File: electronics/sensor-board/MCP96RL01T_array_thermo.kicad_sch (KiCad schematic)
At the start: 54 parts, among them J10 Therm_1, J11 Therm_4, J12 Therm_7, J13 Therm_2, J14 Therm_5, J15 Therm_3, J16 Therm_6, U10 MCP96RL01T, U4 MCP96RL01T, U5 MCP96RL01T, U6 MCP96RL01T, U7 MCP96RL01T, U8 MCP96RL01T, U9 MCP96RL01T

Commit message: work on sensor-board
thermocouple connector footprints made (selected connector)
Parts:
- J10, J11, J12, J13, J14, J15, J16: footprint (none) -> K_type_thermo_conn_F:K_type_thermo_conn_F
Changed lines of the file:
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@@
     (property "Reference" "J10" (id 0) (at 26.162 40.005 0))
     (property "Value" "Therm_1" (id 1) (at 27.432 48.895 0))
-    (property "Footprint" "" (id 2) (at 25.4 42.545 0)
+    (property "Footprint" "K_type_thermo_conn_F:K_type_thermo_conn_F" (id 2) (at 25.4 42.545 0)
       (effects (font (size 1.27 1.27)) hide)
     )
@@
     (property "Reference" "J11" (id 0) (at 26.162 95.885 0))
     (property "Value" "Therm_4" (id 1) (at 27.432 104.775 0))
-    (property "Footprint" "" (id 2) (at 25.4 98.425 0)
+    (property "Footprint" "K_type_thermo_conn_F:K_type_thermo_conn_F" (id 2) (at 25.4 98.425 0)
       (effects (font (size 1.27 1.27)) hide)
     )
@@
     (property "Reference" "J12" (id 0) (at 81.407 151.765 0))
     (property "Value" "Therm_7" (id 1) (at 82.677 160.655 0))
-    (property "Footprint" "" (id 2) (at 80.645 154.305 0)
+    (property "Footprint" "K_type_thermo_conn_F:K_type_thermo_conn_F" (id 2) (at 80.645 154.305 0)
       (effects (font (size 1.27 1.27)) hide)
     )
@@
     (property "Reference" "J13" (id 0) (at 108.077 40.005 0))
     (property "Value" "Therm_2" (id 1) (at 109.347 48.895 0))
-    (property "Footprint" "" (id 2) (at 107.315 42.545 0)
+    (property "Footprint" "K_type_thermo_conn_F:K_type_thermo_conn_F" (id 2) (at 107.315 42.545 0)
       (effects (font (size 1.27 1.27)) hide)
     )
@@
     (property "Reference" "J14" (id 0) (at 108.077 95.885 0))
     (property "Value" "Therm_5" (id 1) (at 109.347 104.775 0))
-    (property "Footprint" "" (id 2) (at 107.315 98.425 0)
+    (property "Footprint" "K_type_thermo_conn_F:K_type_thermo_conn_F" (id 2) (at 107.315 98.425 0)
       (effects (font (size 1.27 1.27)) hide)
     )
@@
     (property "Reference" "J15" (id 0) (at 189.992 40.005 0))
     (property "Value" "Therm_3" (id 1) (at 191.262 48.895 0))
-    (property "Footprint" "" (id 2) (at 189.23 42.545 0)
+    (property "Footprint" "K_type_thermo_conn_F:K_type_thermo_conn_F" (id 2) (at 189.23 42.545 0)
       (effects (font (size 1.27 1.27)) hide)
     )
@@
     (property "Reference" "J16" (id 0) (at 189.992 95.885 0))
     (property "Value" "Therm_6" (id 1) (at 191.262 104.775 0))
-    (property "Footprint" "" (id 2) (at 189.23 98.425 0)
+    (property "Footprint" "K_type_thermo_conn_F:K_type_thermo_conn_F" (id 2) (at 189.23 98.425 0)
       (effects (font (size 1.27 1.27)) hide)
     )

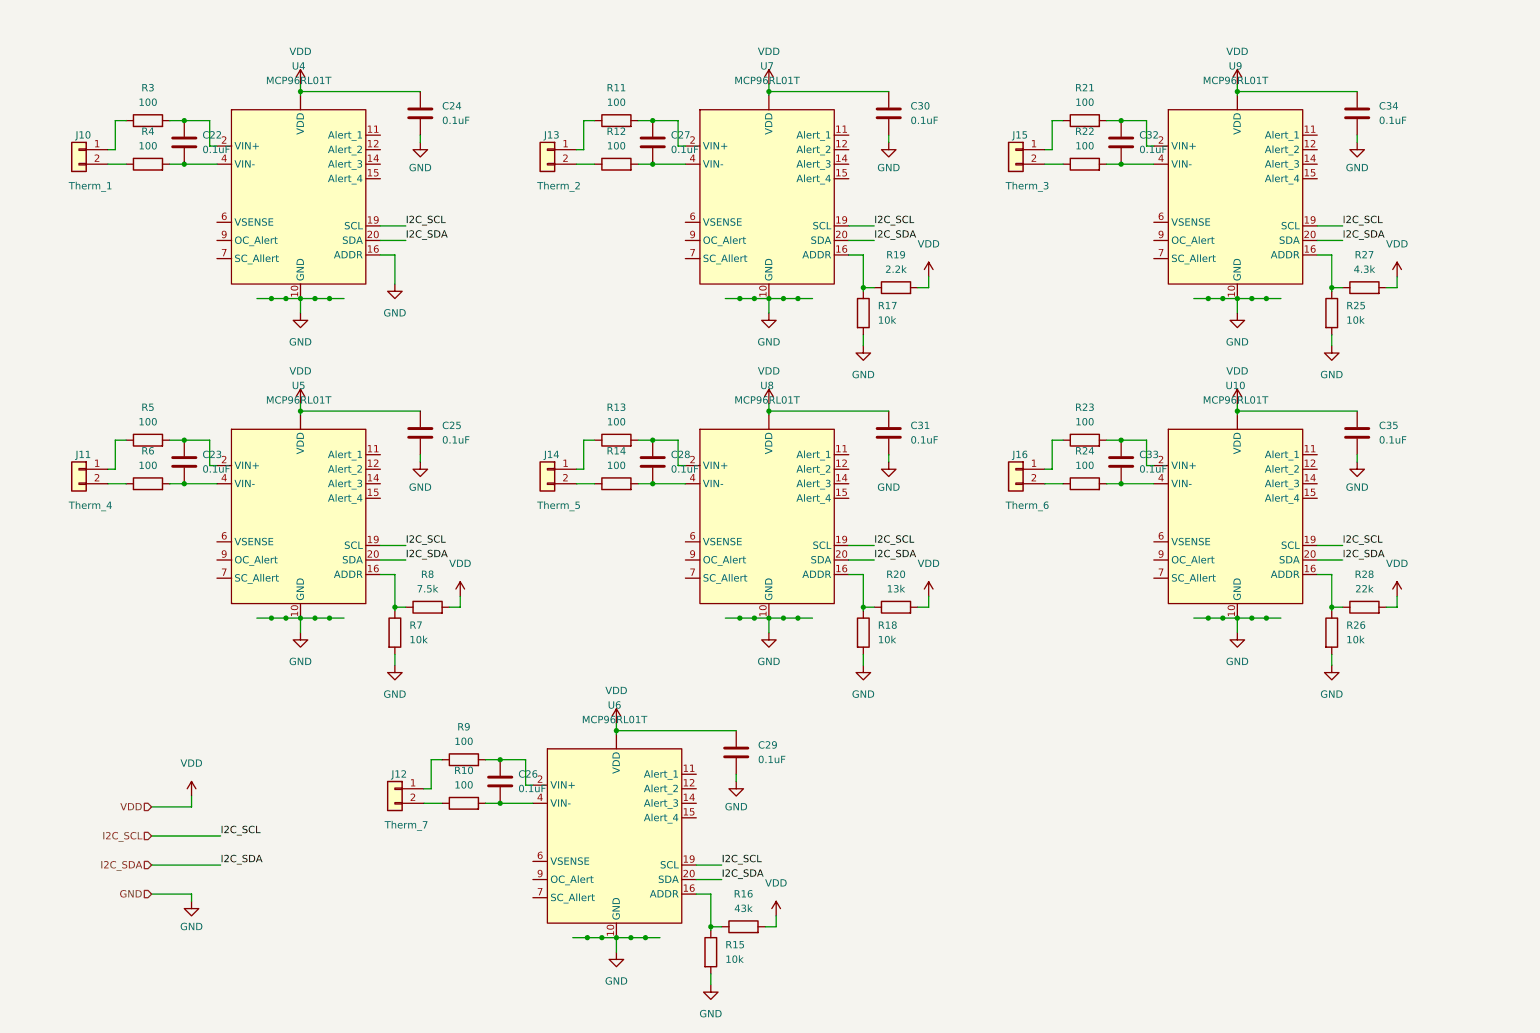
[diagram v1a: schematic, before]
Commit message: work on sensor-board
finishing sub-circuits
switching mcu to stm32f105
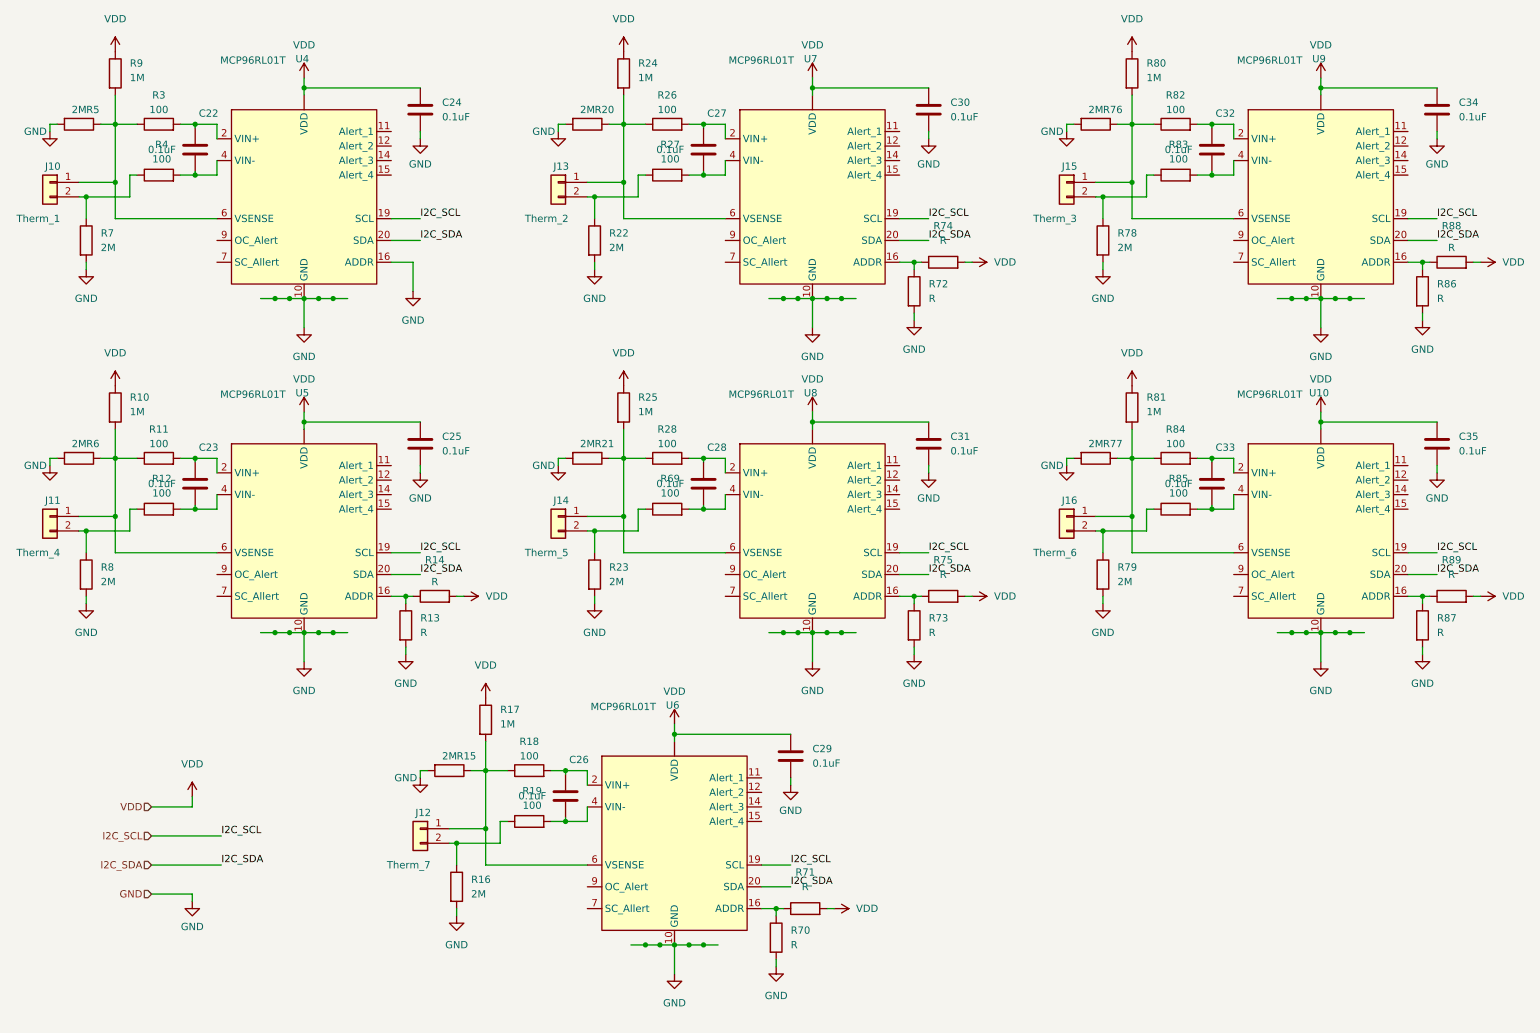
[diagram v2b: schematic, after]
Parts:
- added R69, R82, R83, R84, R85: 100, Resistor_SMD:R_0603_1608Metric, symbol Device:R
- added R70, R71, R72, R73, R74, R75, R86, R87, R88, R89: R, Resistor_SMD:R_0603_1608Metric, symbol Device:R
- added R76, R77, R78, R79: 2M, Resistor_SMD:R_0603_1608Metric, symbol Device:R
- added R80, R81: 1M, Resistor_SMD:R_0603_1608Metric, symbol Device:R
- R10, R24, R9: value 100 -> 1M
- R13, R14: value 100 -> R
- R15, R7: value 10k -> 2M
- R16: value 43k -> 2M
- R17, R25: value 10k -> 1M
- R18, R26: value 10k -> 100
- R19: value 2.2k -> 100
- R20: value 13k -> 2M
- R21, R22, R23, R5, R6: value 100 -> 2M
- R27: value 4.3k -> 100
- R28: value 22k -> 100
- R8: value 7.5k -> 2M
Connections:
- net GND: now also R13.2, R16.2, R20.2, R21.2, R22.2, R23.2, R5.2, R6.2, R8.2, R70.2, R72.2, R73.2, R76.2, R77.2, R78.2, R79.2, R86.2, R87.2; no longer R17.2, R18.2, R25.2, R26.2
- net VDD: now also R10.1, R14.2, R17.1, R24.1, R25.1, R9.1, R71.2, R74.2, R75.2, R80.1, R81.1, R88.2, R89.2; no longer R16.2, R19.2, R20.2, R27.2, R28.2, R8.2
- net at J10.2 (Pin_2), R4.1: now also R7.1
- net at R13.1: now also R14.1, U5.16 (ADDR); no longer J14.1 (Pin_1)
- net at C28.1, U8.2 (VIN+): now also R28.2; no longer R13.2
- net at C32.1, U9.2 (VIN+): now also R82.2; no longer R21.2
- net at C32.2, U9.4 (VIN-): now also R83.2; no longer R22.2
- net at R22.1: now also J13.2 (Pin_2), R27.1; no longer J15.2 (Pin_2)
- net at C33.1, U10.2 (VIN+): now also R84.2; no longer R23.2
- net at C33.2, U10.4 (VIN-): now also R85.2; no longer R24.2
- net at J16.1 (Pin_1): now also U10.6 (VSENSE), R77.1, R81.2, R84.1; no longer R23.1
- net at J14.2 (Pin_2): now also R23.1, R69.1; no longer R14.1
- net at C28.2, U8.4 (VIN-): now also R69.2; no longer R14.2
- net at U8.6 (VSENSE): now also J14.1 (Pin_1), R21.1, R25.2, R28.1
- net at C23.1, U5.2 (VIN+): now also R11.2; no longer R5.2
- net at C23.2, U5.4 (VIN-): now also R12.2; no longer R6.2
- net at U5.6 (VSENSE): now also J11.1 (Pin_1), R10.2, R11.1, R6.1
- net at J12.1 (Pin_1): now also R15.1, R17.2, R18.1, U6.6 (VSENSE); no longer R9.1
- net at J12.2 (Pin_2): now also R16.1, R19.1; no longer R10.1
- net at C27.1, U7.2 (VIN+): now also R26.2; no longer R11.2
- net at C27.2, U7.4 (VIN-): now also R27.2; no longer R12.2
- net at J11.2 (Pin_2): now also R12.1, R8.1; no longer R6.1
- net at J13.1 (Pin_1): now also R20.1, R24.2, R26.1, U7.6 (VSENSE); no longer R11.1
- net at J10.1 (Pin_1), R3.1: now also R5.1, R9.2, U4.6 (VSENSE)
- net at U9.6 (VSENSE): now also J15.1 (Pin_1), R76.1, R80.2, R82.1
- net at J16.2 (Pin_2): now also R79.1, R85.1; no longer R24.1
- net at C26.1, U6.2 (VIN+): now also R18.2; no longer R9.2
- net at C26.2, U6.4 (VIN-): now also R19.2; no longer R10.2
- new net: R70.1, R71.1, U6.16 (ADDR)
- new net: R72.1, R74.1, U7.16 (ADDR)
- new net: R87.1, R89.1, U10.16 (ADDR)
- new net: R86.1, R88.1, U9.16 (ADDR)
- new net: J15.2 (Pin_2), R78.1, R83.1
- new net: R73.1, R75.1, U8.16 (ADDR)
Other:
- moved on the sheet: C22, C24, J10, R3, R4, U4

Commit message: Finalized sensor-board schematic
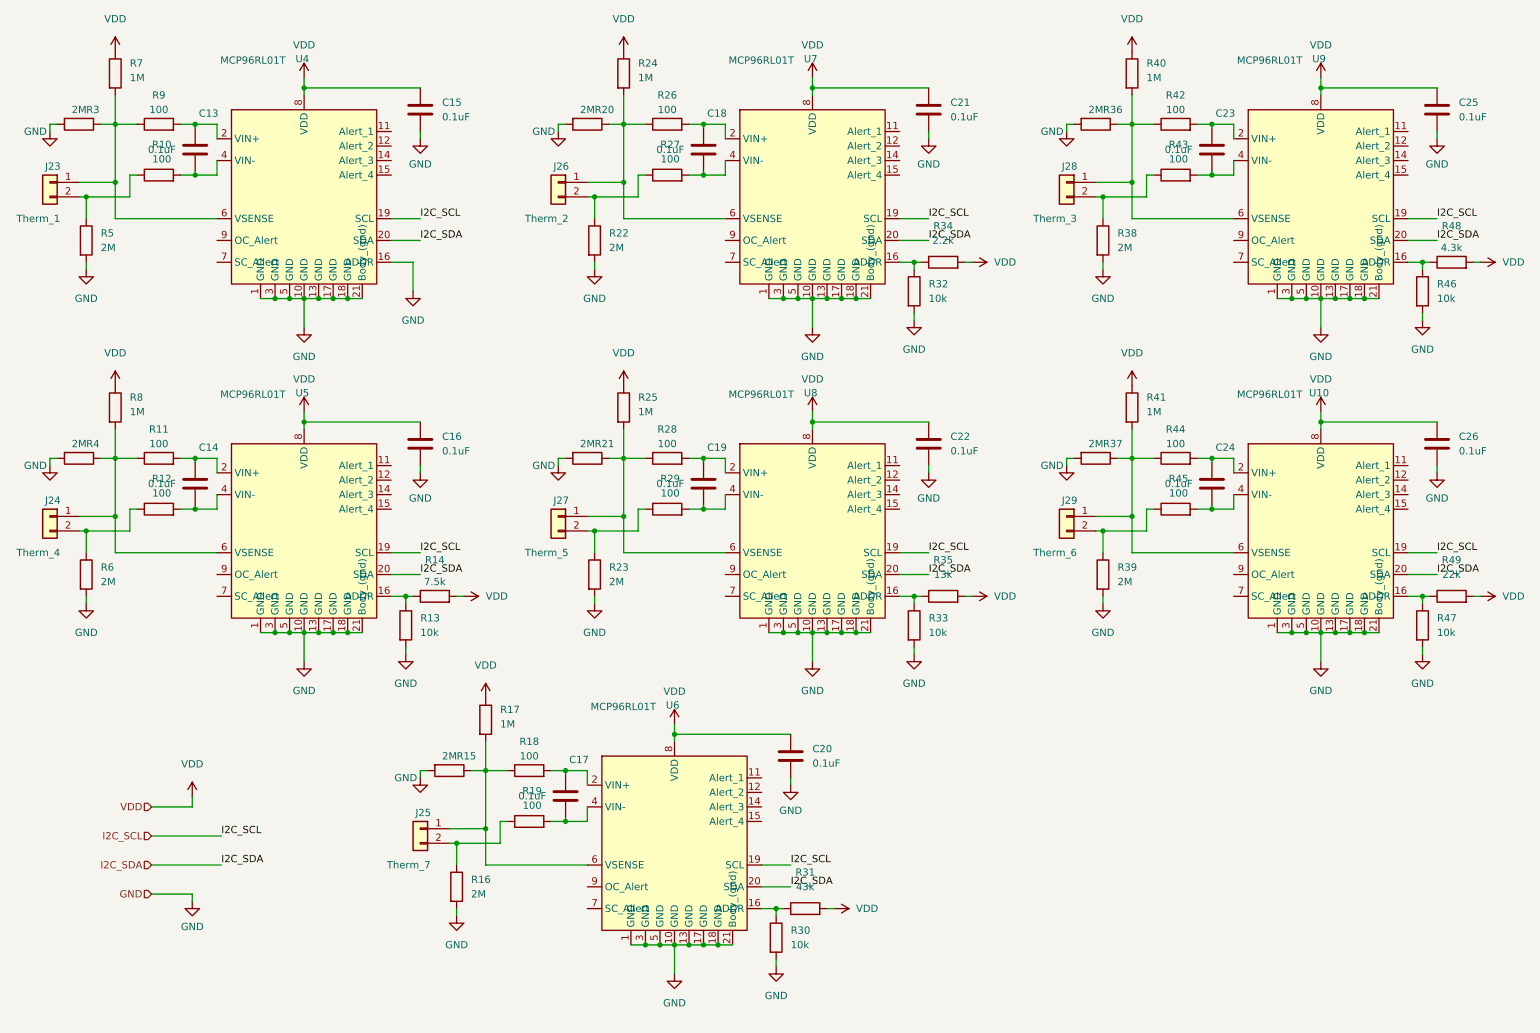
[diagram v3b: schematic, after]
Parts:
- R13: value R -> 10k
- R14: value R -> 7.5k
- R30: renamed from R70; value R -> 10k
- R31: renamed from R71; value R -> 43k
- R32: renamed from R72; value R -> 10k
- R33: renamed from R73; value R -> 10k
- R34: renamed from R74; value R -> 2.2k
- R35: renamed from R75; value R -> 13k
- R46: renamed from R86; value R -> 10k
- R47: renamed from R87; value R -> 10k
- R48: renamed from R88; value R -> 4.3k
- R49: renamed from R89; value R -> 22k
- renumbered C22 to C13, C23 to C14, C24 to C15, C25 to C16, C26 to C17, C27 to C18, C28 to C19, C29 to C20, C30 to C21, C31 to C22, C32 to C23, C33 to C24, C34 to C25, C35 to C26, J10 to J23, J11 to J24, J12 to J25, J13 to J26, J14 to J27, J15 to J28, J16 to J29, R4 to R10, R69 to R29, R5 to R3, R76 to R36, R77 to R37, R78 to R38, R79 to R39, R6 to R4, R80 to R40, R81 to R41, R82 to R42, R83 to R43, R84 to R44, R85 to R45, R7 to R5, R8 to R6, R9 to R7, R10 to R8, R3 to R9
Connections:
- net GND: now also U10.21 (Body_(gnd)), U4.21 (Body_(gnd)), U5.21 (Body_(gnd)), U6.21 (Body_(gnd)), U7.21 (Body_(gnd)), U8.21 (Body_(gnd)), U9.21 (Body_(gnd))
- net VDD: now also U10.8 (VDD), U4.8 (VDD), U5.8 (VDD), U6.8 (VDD), U7.8 (VDD), U8.8 (VDD), U9.8 (VDD); no longer U10. (VDD), U4. (VDD), U5. (VDD), U6. (VDD), U7. (VDD), U8. (VDD), U9. (VDD)
